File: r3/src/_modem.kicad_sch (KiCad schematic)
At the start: 37 parts, among them J1 , J11 SMA, J12 U_FL-R-SMT-1_10_, J13 JAE_SIM_Card_SF72S006, J2 , J3 , J4 , J5 , J6 , J7 , J8 , J9 , T10 , T11 , T8 , T9 , U7 Sierra_Wireless_RC7620, U8 ESD7004, U9 TXS0108EPW

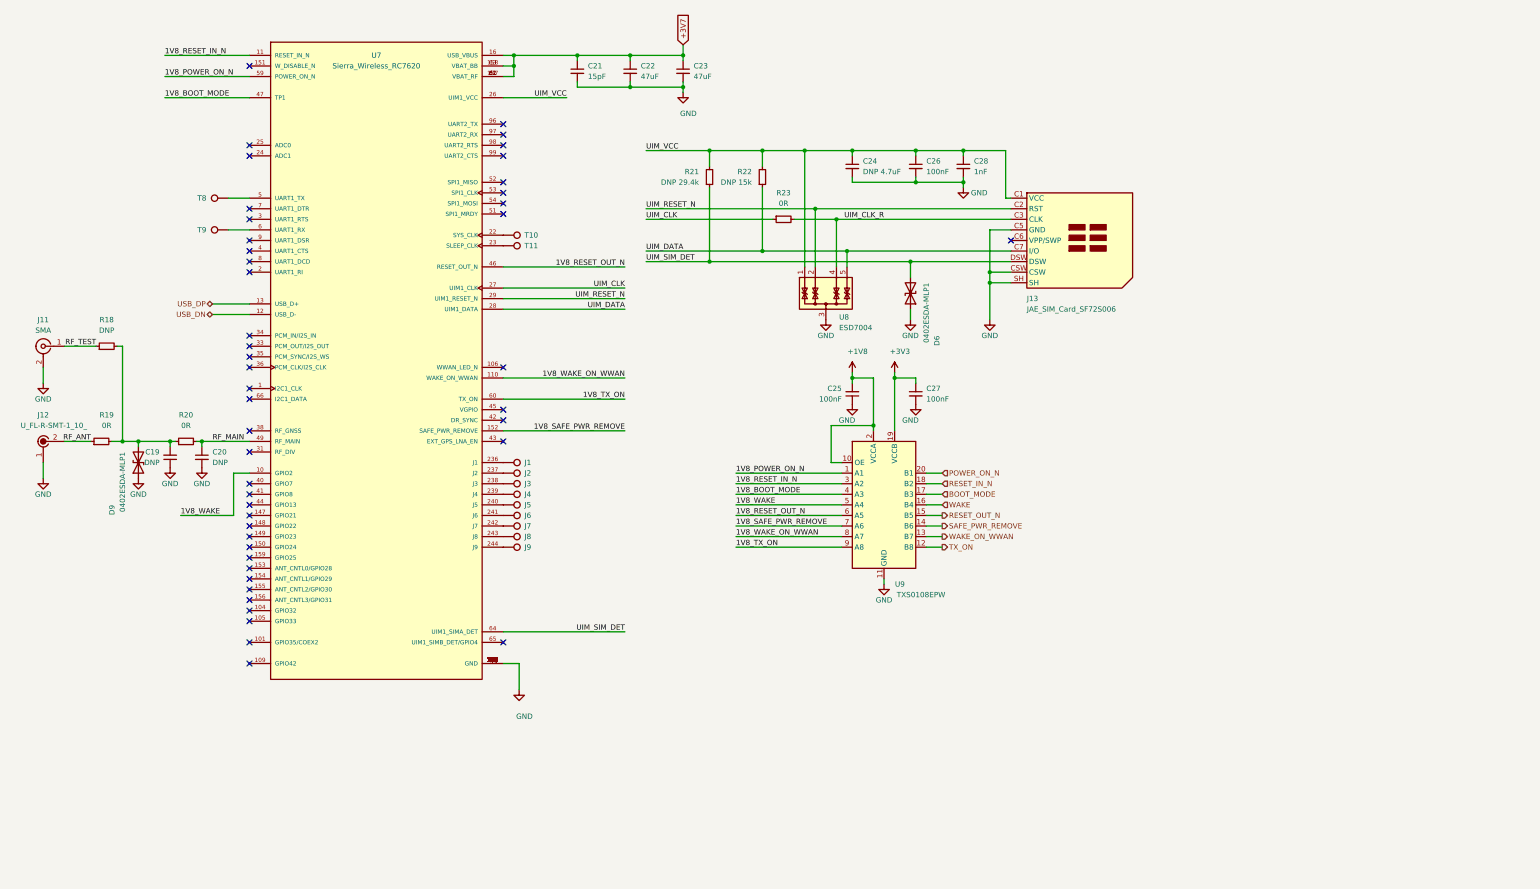
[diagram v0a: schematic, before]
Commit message: Replace fancy level tranlator, which pissed off the modem, with a simple bunch of FETs
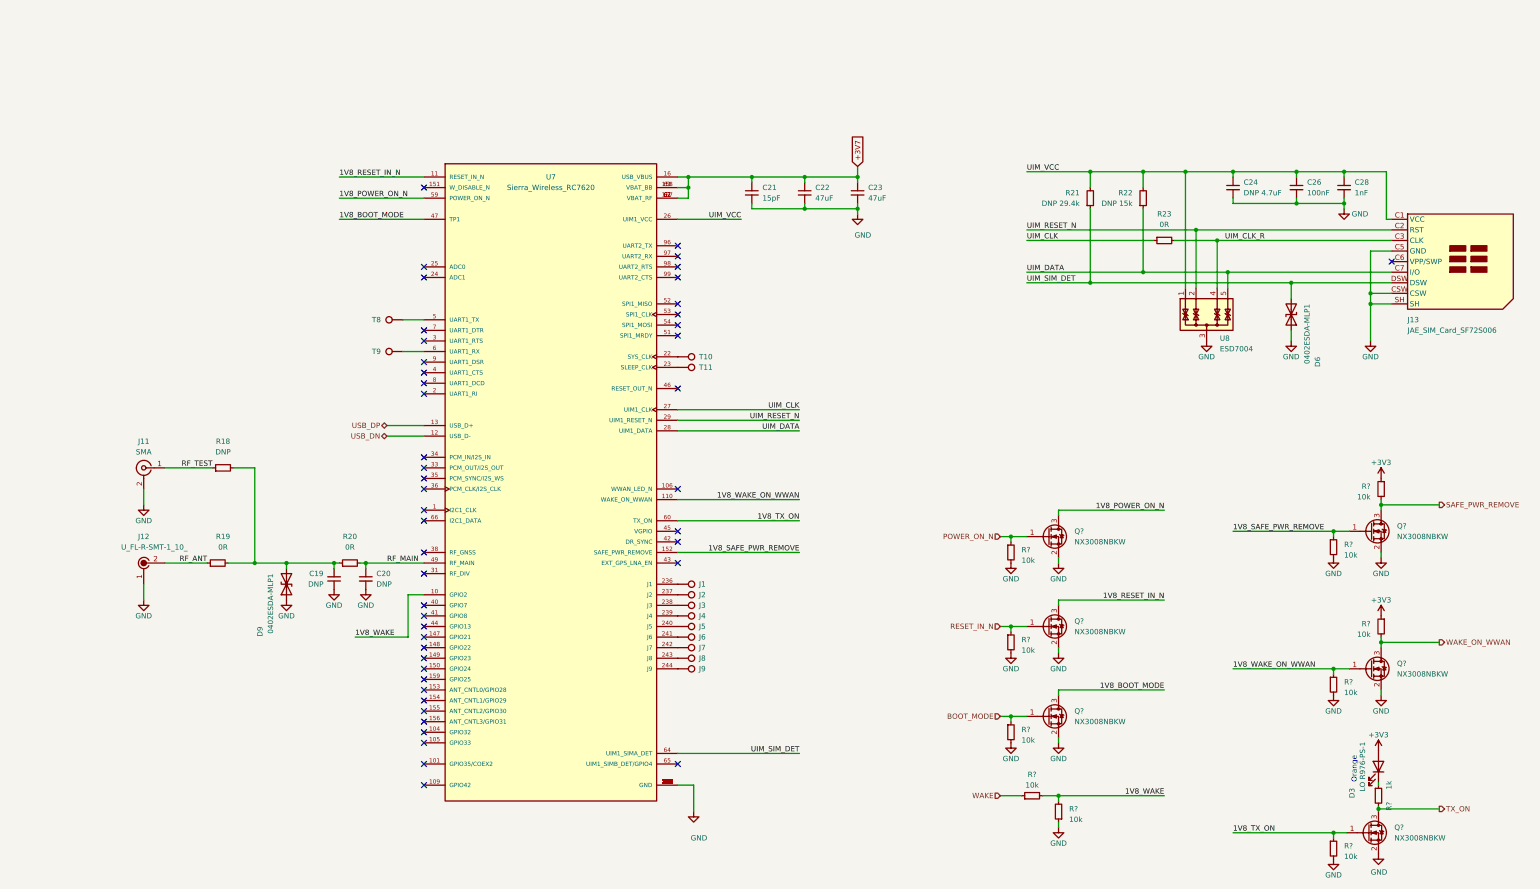
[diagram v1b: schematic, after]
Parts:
- removed C25, C27: 100nF, Capacitor_SMD:C_0603_1608Metric, symbol Device:C_Small
- removed U9: TXS0108EPW, Package_SO:TSSOP-20_4.4x6.5mm_P0.65mm, symbol Logic_LevelTranslator:TXS0108EPW
- added D3: LO R976-PS-1, jeffmakes-footprints:CHIPLED-0805, symbol Device:LED
- added Q? (x6): NX3008NBKW, Package_TO_SOT_SMD:SOT-323_SC-70, symbol Device:Q_NMOS_GSD
- added R? (x10): 10k, Resistor_SMD:R_0603_1608Metric, symbol Device:R_Small
- added R?: 1k, Resistor_SMD:R_0603_1608Metric, symbol Device:R_Small
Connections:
- net +3V3: now also D3.2 (A), R?.1, R?.1
- net 1V8_BOOT_MODE: now also Q?.3 (D)
- net 1V8_POWER_ON_N: now also Q?.3 (D)
- net 1V8_RESET_IN_N: now also Q?.3 (D)
- net 1V8_SAFE_PWR_REMOVE: now also Q?.1 (G), R?.1
- net 1V8_TX_ON: now also Q?.1 (G), R?.1
- net 1V8_WAKE: now also R?.2, R?.2
- net 1V8_WAKE_ON_WWAN: now also Q?.1 (G), R?.1
- net BOOT_MODE: now also Q?.1 (G), R?.1
- net GND: now also Q?.2 (S), Q?.2 (S), Q?.2 (S), Q?.2 (S), Q?.2 (S), Q?.2 (S), R?.1, R?.2, R?.2, R?.2, R?.2, R?.2, R?.2
- net POWER_ON_N: now also Q?.1 (G), R?.1
- net RESET_IN_N: now also Q?.1 (G), R?.1
- net SAFE_PWR_REMOVE: now also Q?.3 (D), R?.2
- net TX_ON: now also Q?.3 (D), R?.2
- net WAKE: now also R?.1
- net WAKE_ON_WWAN: now also Q?.3 (D), R?.2
- net 1V8_RESET_OUT_N: no longer names the net of U7.46 (RESET_OUT_N)
- new net: D3.1 (K), R?.1
- no-connect marks 47 -> 48
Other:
- note added: "Orange"
- moved on the sheet: C19, C20, C21, C22, C23, C24, C26, C28, D6, D9, J1, J11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
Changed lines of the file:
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@@
 (kicad_sch (version 20210406) (generator eeschema)
-  (paper "A4")
+  (paper "A3")

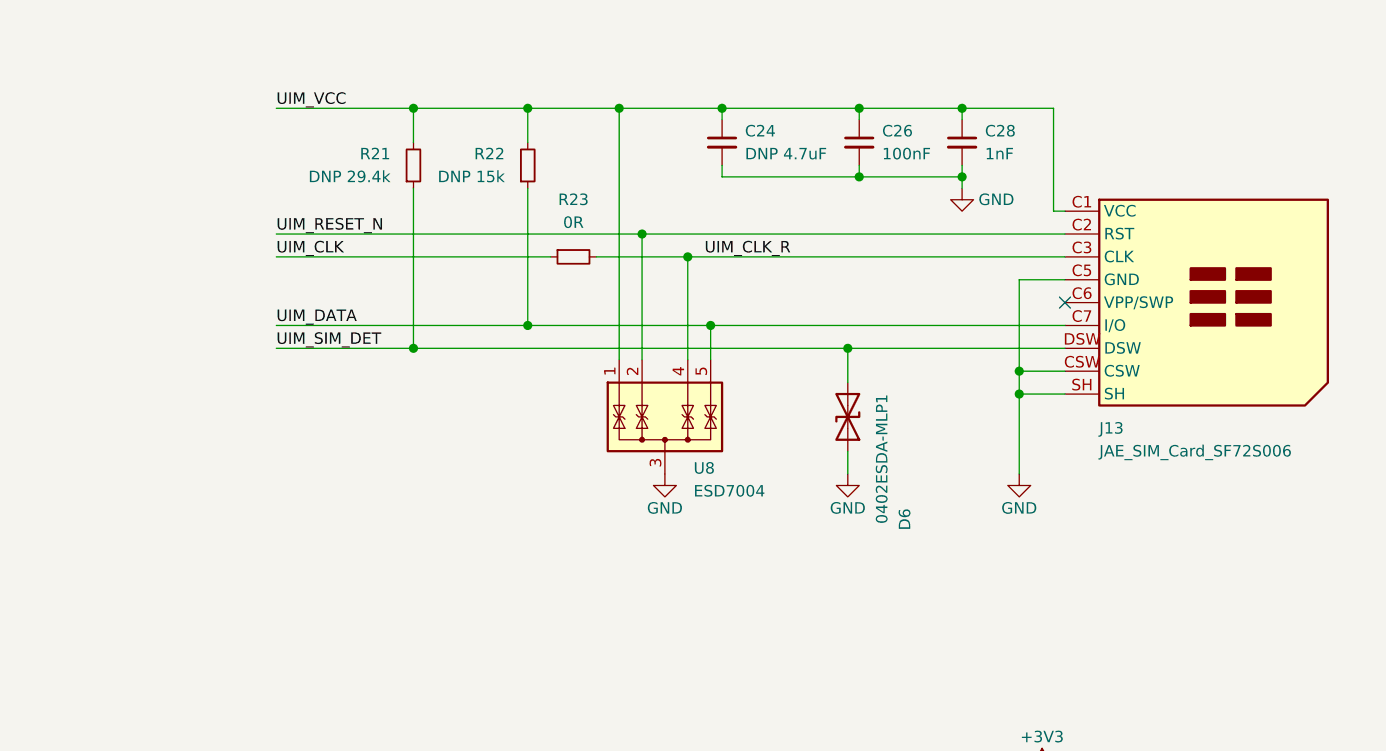
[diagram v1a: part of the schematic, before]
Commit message: Invert SIM detect signal
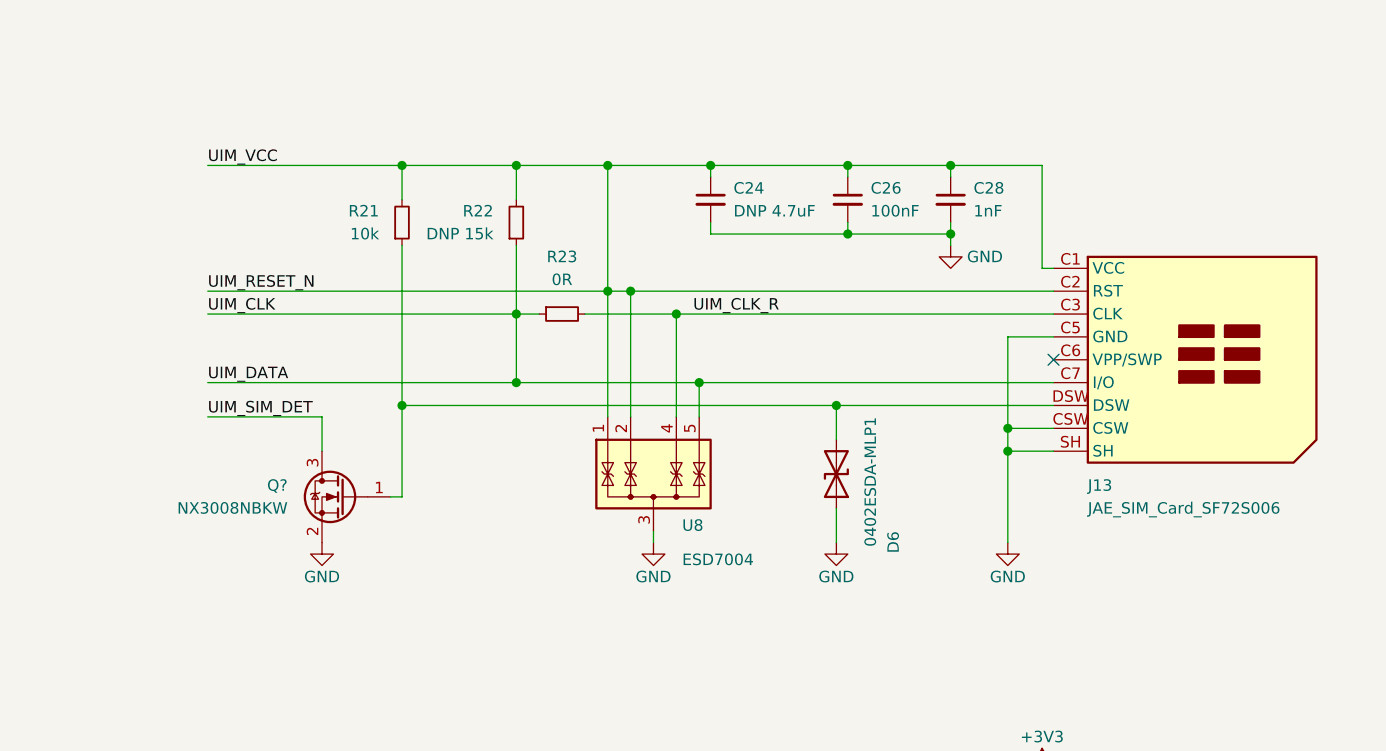
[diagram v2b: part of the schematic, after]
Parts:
- added Q?: NX3008NBKW, Package_TO_SOT_SMD:SOT-323_SC-70, symbol Device:Q_NMOS_GSD
- R21: value DNP 29.4k -> 10k
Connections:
- net UIM_DATA is gone; now on net UIM_CLK: J13.C7 (I/O), R22.1, U7.28 (UIM1_DATA), U8.5 (IO4)
- net UIM_VCC is gone; now on net UIM_RESET_N: C24.1, C26.1, C28.1, J13.C1 (VCC), R21.2, R22.2, U7.26 (UIM1_VCC), U8.1 (IO1)
- net GND: now also Q?.2 (S)
- net UIM_SIM_DET: now also Q?.3 (D); no longer D6.2 (A2), J13.DSW, R21.1
- new net: D6.2 (A2), J13.DSW, Q?.1 (G), R21.1
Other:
- moved on the sheet: C24, C26, C28, D6, J13, R21, R22, R23, U8

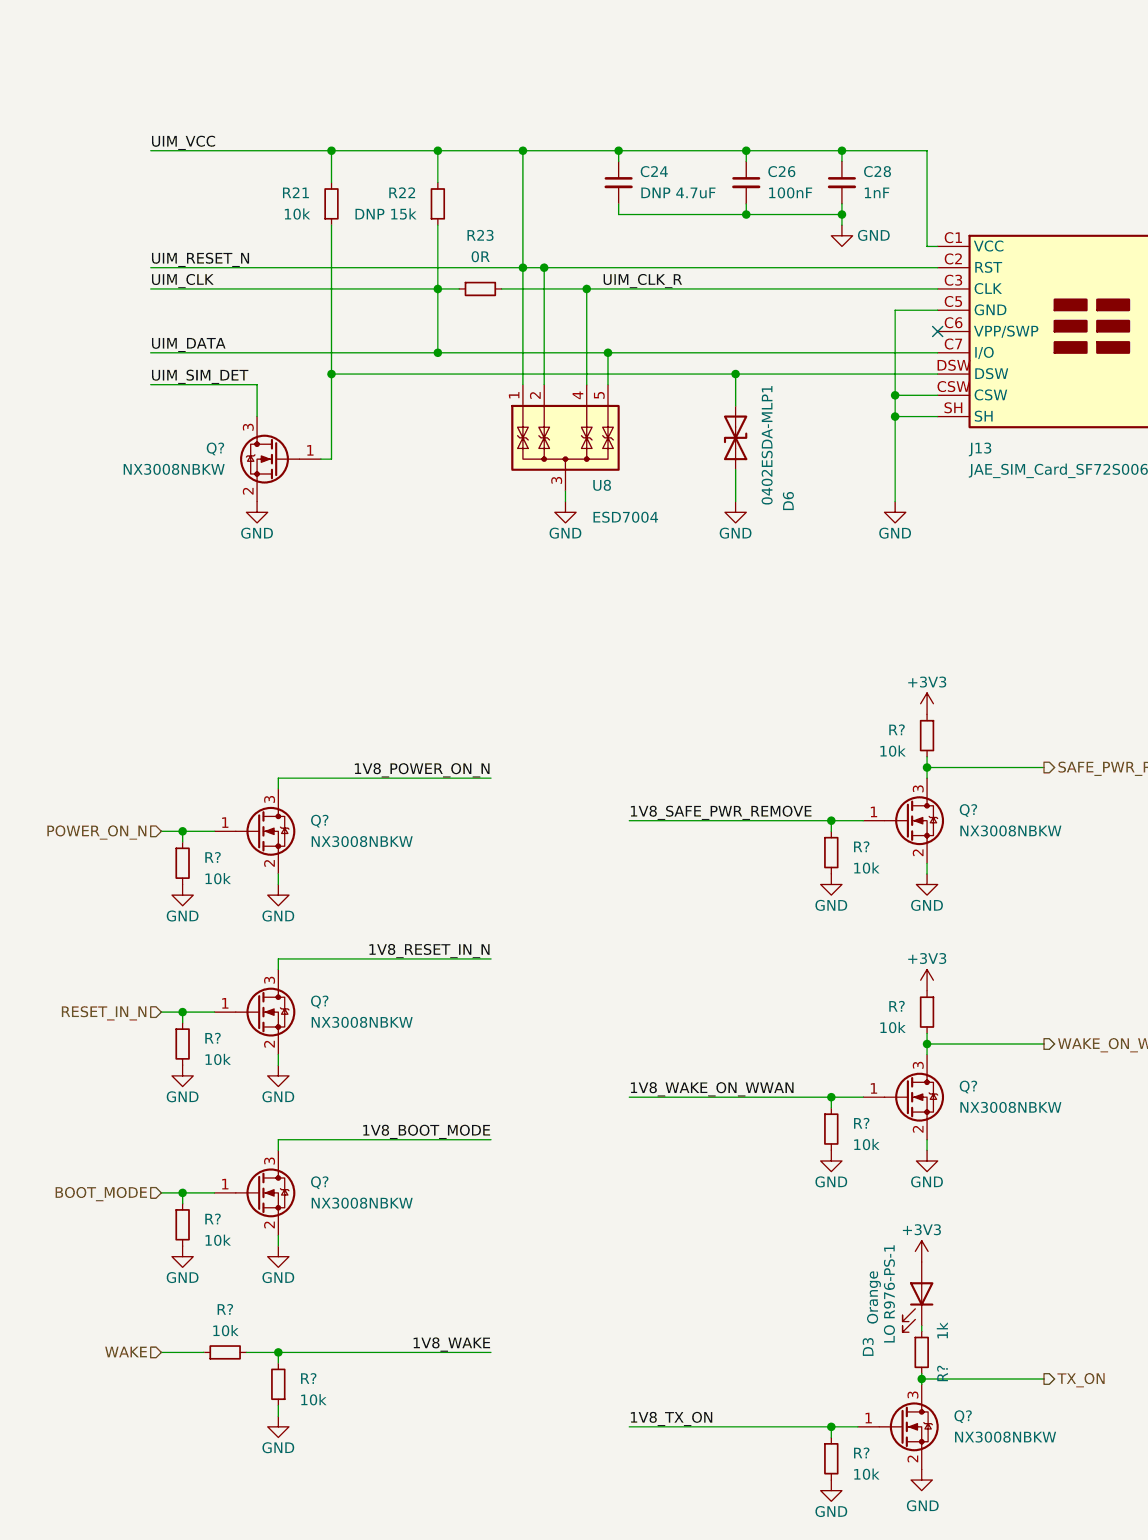
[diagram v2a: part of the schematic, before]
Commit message: Fix ERC error - had a stray wire junction shorting some things
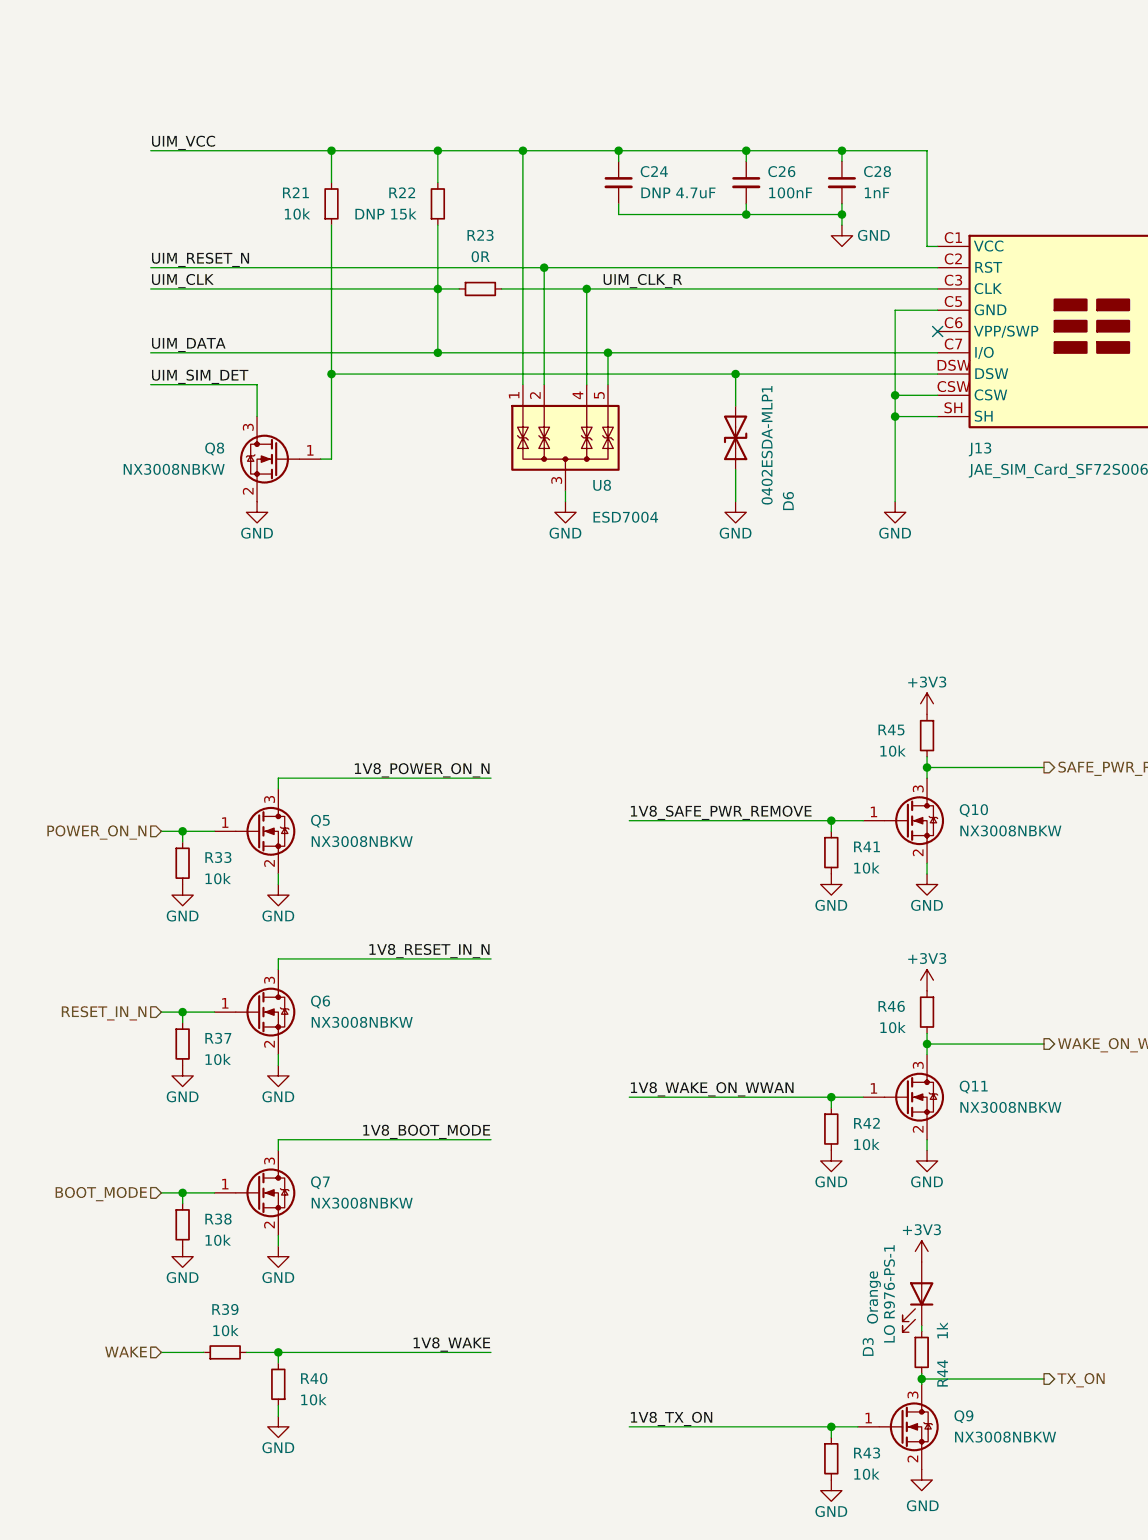
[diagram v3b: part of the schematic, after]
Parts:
- gave numbers to parts that had none: 18
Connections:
- net UIM_RESET_N: no longer C24.1, C26.1, C28.1, J13.C1 (VCC), R21.2, R22.2, U7.26 (UIM1_VCC), U8.1 (IO1)
- new net UIM_VCC: C24.1, C26.1, C28.1, J13.C1 (VCC), R21.2, R22.2, U7.26 (UIM1_VCC), U8.1 (IO1)

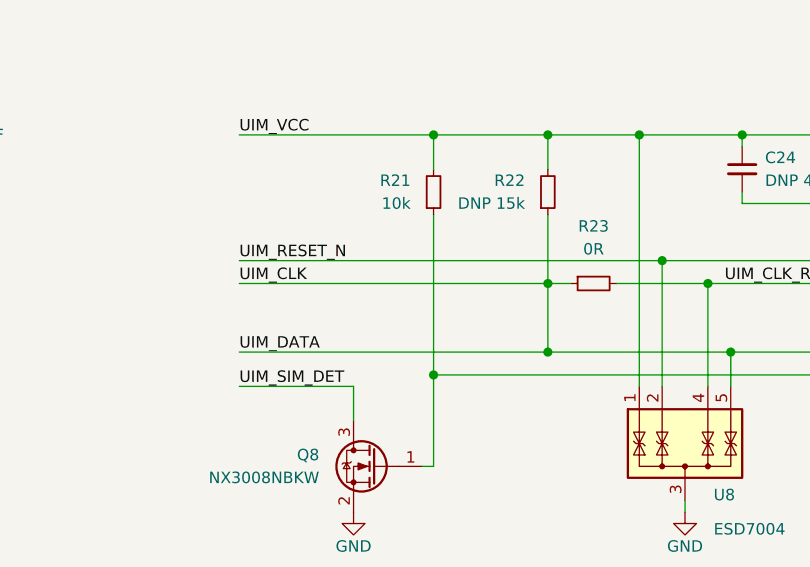
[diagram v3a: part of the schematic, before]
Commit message: Remove stray junction. Lethal!
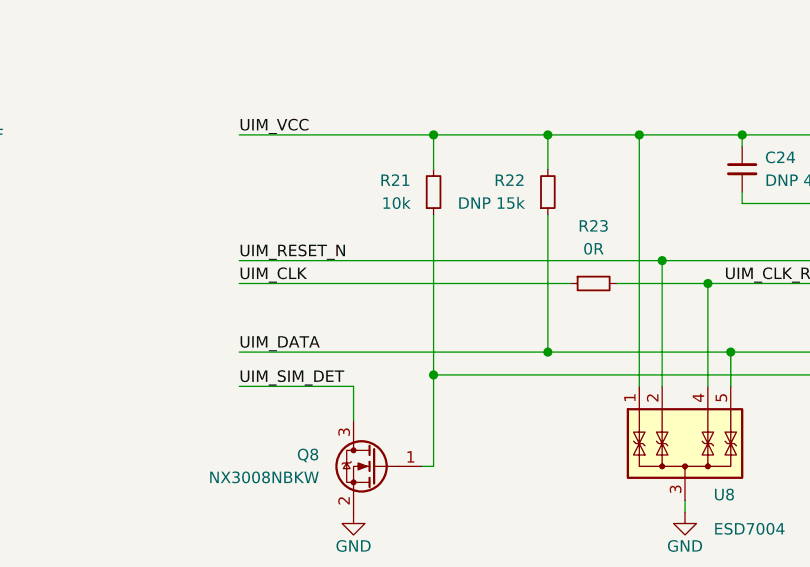
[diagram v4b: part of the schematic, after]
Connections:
- net UIM_CLK: no longer J13.C7 (I/O), R22.1, U7.28 (UIM1_DATA), U8.5 (IO4)
- new net UIM_DATA: J13.C7 (I/O), R22.1, U7.28 (UIM1_DATA), U8.5 (IO4)

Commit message: Change to new 5-pin variant of the protection diode network symbol
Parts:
- U8: footprint jeffmakes-footprints:USON-10_2.5x1.0mm_P0.5mm -> Package_SON:USON-10_2.5x1.0mm_P0.5mm; symbol Power_Protection:TPD4E02B04DQA -> j_Power_Protection:ESD7004
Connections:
- net GND: no longer U8.8 (G)

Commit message: Change all diode protection networks to a 5-pin variant to prevent DRC errors due to missing pads
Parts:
- U8: footprint Package_SON:USON-10_2.5x1.0mm_P0.5mm -> jeffmakes-footprints:USON-10_2.5x1.0mm_P0.5mm
